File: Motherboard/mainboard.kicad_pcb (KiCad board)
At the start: 4 copper layers, 45 x 35 mm, 48 parts, among them IC1 BMX160, J1 Conn_01x01, J2 10118194-0001LF, J28 Conn_01x01, J29 Conn_01x01, J3 Micro_SD_Card, J30 Conn_01x01, J4 xf2m-2415-1a, J5 XF2M-1015-1A, SW1 KMR231NG LFS, U1 RFM95W-915S2, U2 ATSAMD51G_TQFN48, U3 DRV8848, U4 TPS82740BSIPR, U5 DRV8848, U6 MAX708RESA-T, U8 RFM95W-915S2, X1 ANTENNA_U.FL, X2 ANTENNA_U.FL

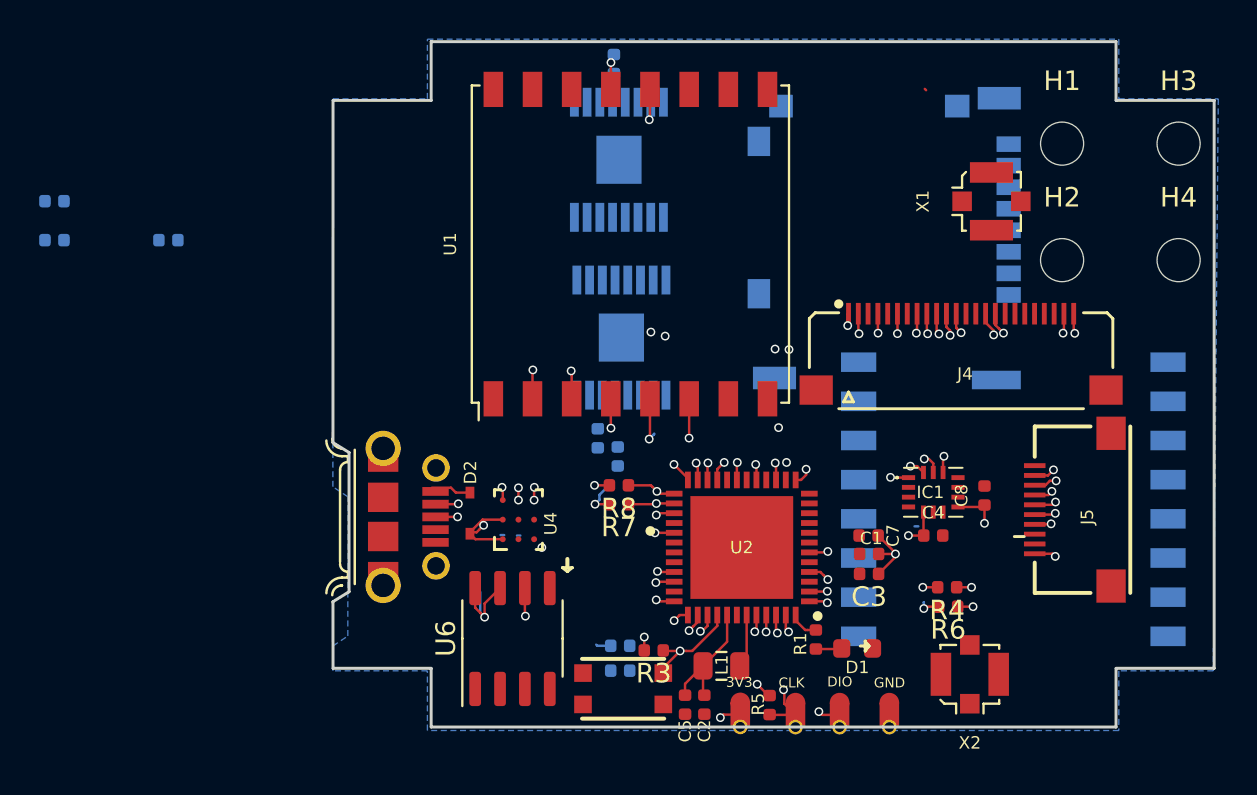
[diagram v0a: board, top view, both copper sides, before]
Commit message: updated H-bridge positions on bottom layer
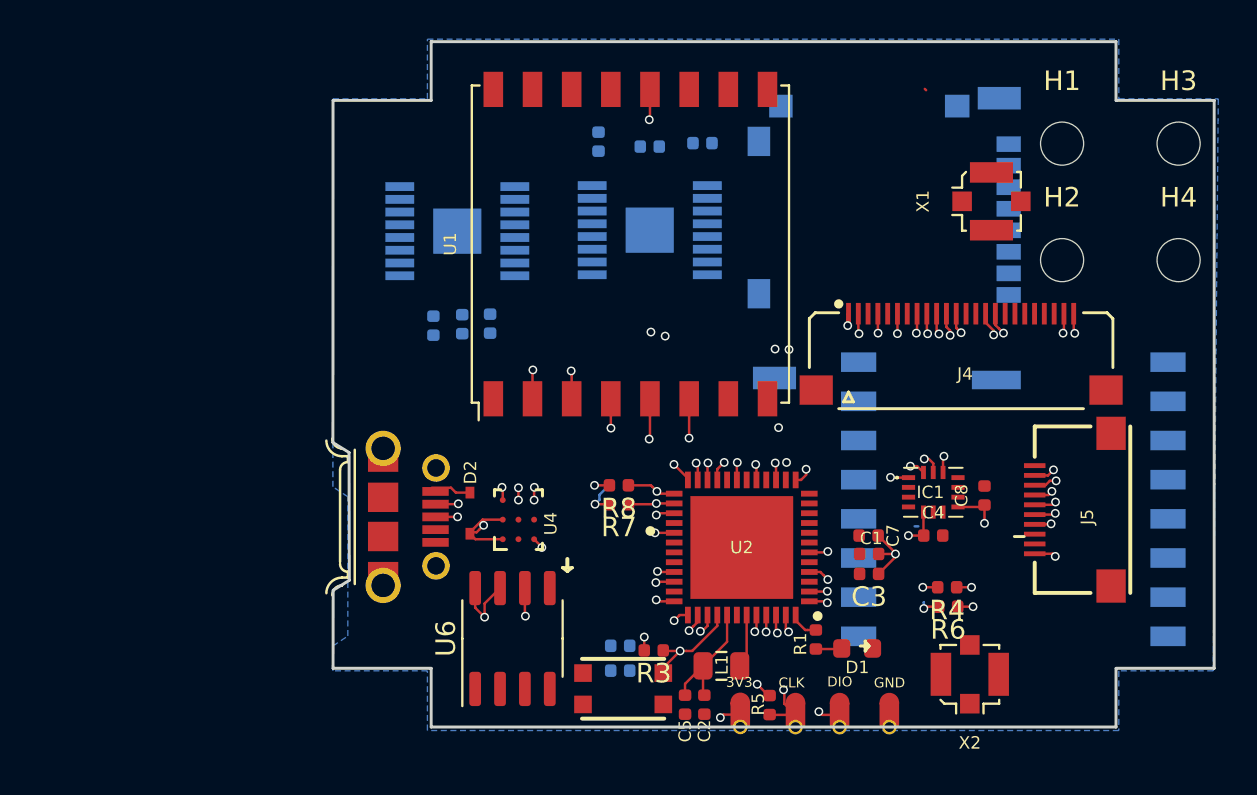
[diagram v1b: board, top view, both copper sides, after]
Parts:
- moved C9 33.5 mm to (95.6, 79.2)
- moved C11 30.5 mm to (92.9, 79.4)
- moved C14 17.0 mm to (84.7, 88.4), turned to 90 degrees
- moved C12 10.4 mm to (83.3, 88.5)
- moved C13 10.2 mm to (81.8, 88.5)
- moved U5 9.99 mm to (83.1, 83.7), turned to 0 degrees
- moved C10 4.04 mm to (90.3, 79.1)
- moved U3 3.92 mm to (92.9, 83.7), turned to 180 degrees
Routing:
- net Net-(C10-Pad1): track 1.50 -> 0.00 mm
- net Net-(R3-Pad2): track 14.3 -> 12.9 mm
- net +3V3: track 21.0 -> 20.2 mm, vias 16 -> 15
- net GND: track 0.79 -> 0.00 mm
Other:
- outline, holes or cut-outs redrawn

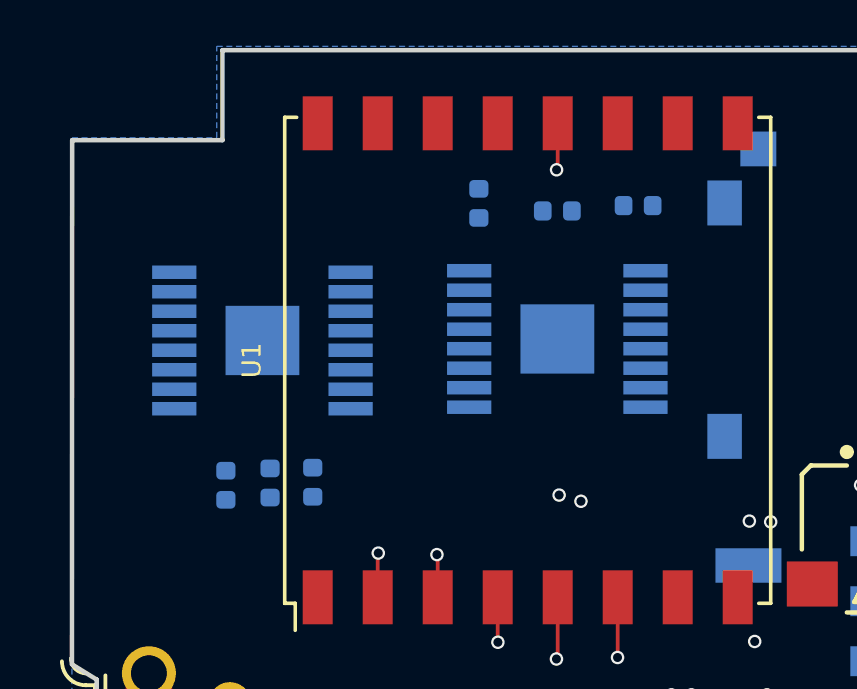
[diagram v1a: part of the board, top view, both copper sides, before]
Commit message: updated H-bridge positions traces with capacitors on bottom layer
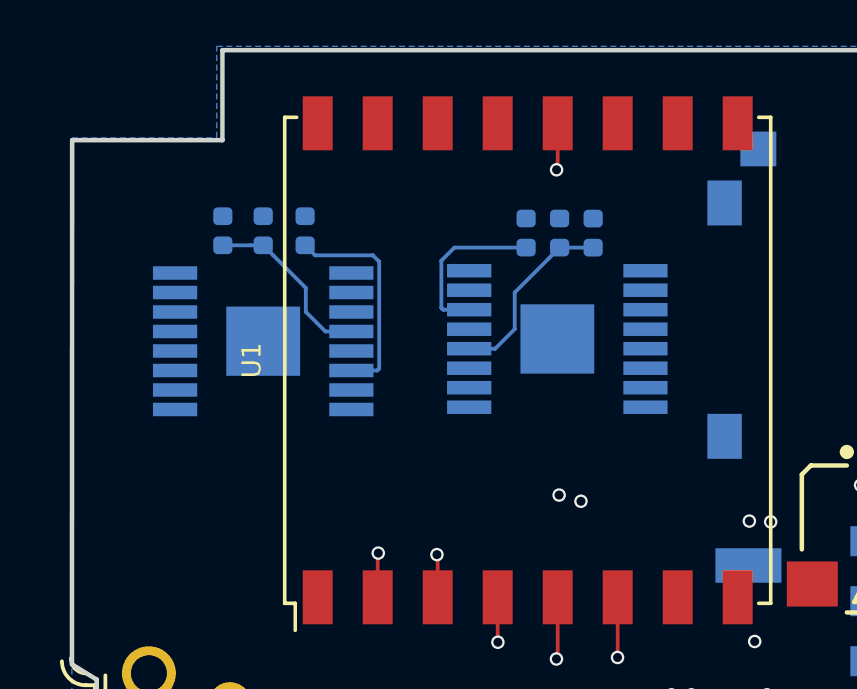
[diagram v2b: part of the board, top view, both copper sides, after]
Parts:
- moved C14 8.90 mm to (81.7, 80.1)
- moved C13 8.89 mm to (84.5, 80.1), turned to 270 degrees
- moved C12 8.41 mm to (83.1, 80.1), turned to 90 degrees
- moved C10 3.94 mm to (94.1, 80.1)
- moved C9 2.77 mm to (93.0, 80.1), turned to 90 degrees
- moved C11 1.28 mm to (91.8, 80.1), turned to 270 degrees
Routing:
- net Net-(C13-Pad2): track 0.00 -> 7.21 mm
- net Net-(C10-Pad1): track 0.00 -> 6.24 mm
- net Net-(C12-Pad1): track 0.00 -> 5.94 mm
- net Net-(C11-Pad2): track 0.00 -> 5.53 mm

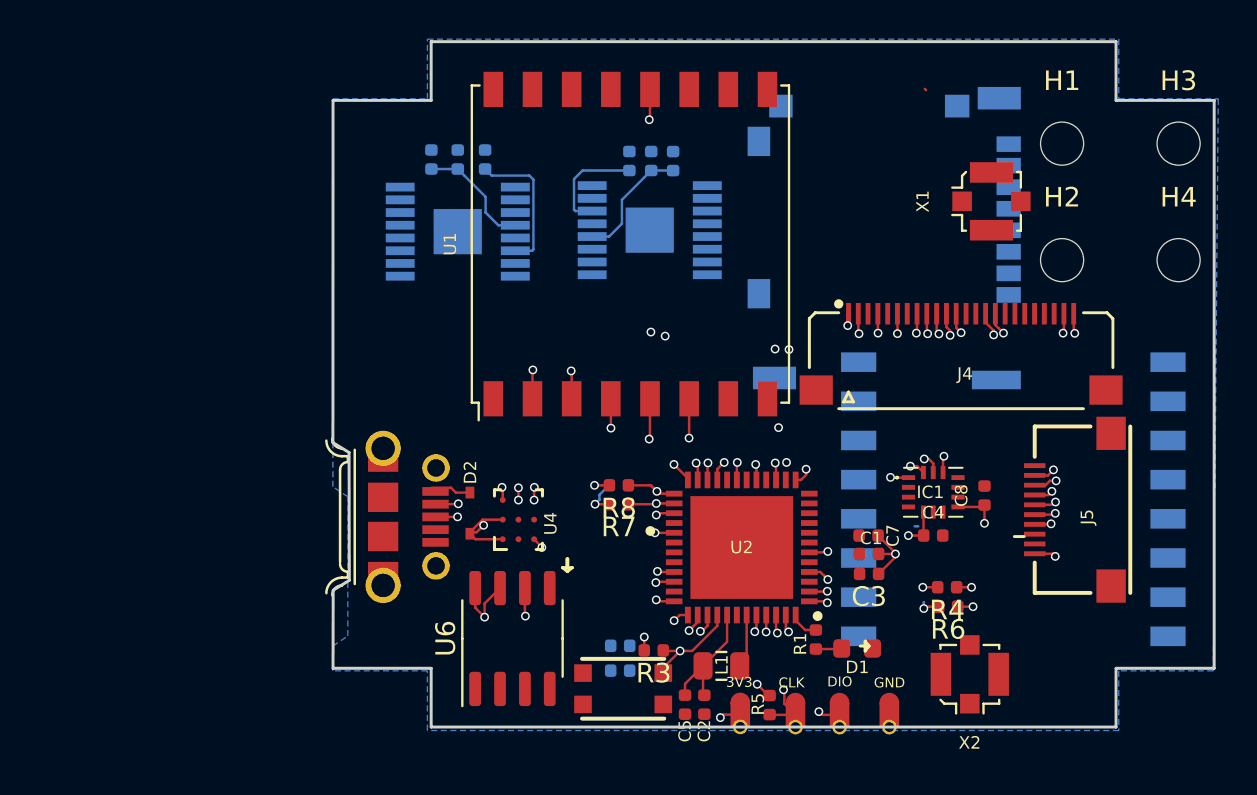
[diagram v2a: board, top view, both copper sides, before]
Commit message: updated traces for UHF and SD card on bottom layer
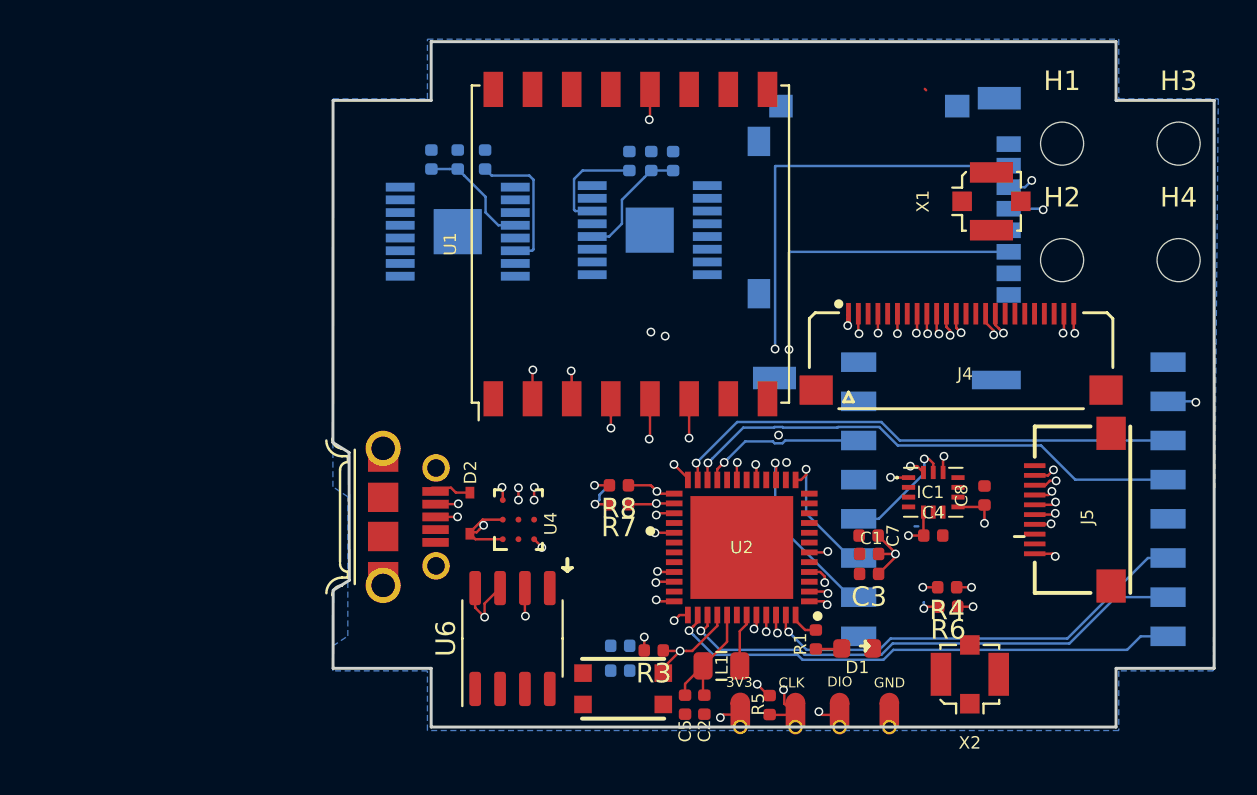
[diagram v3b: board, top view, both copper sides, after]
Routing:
- net MISO: track 38.0 -> 68.2 mm
- net RF_DIO2: track 0.98 -> 26.5 mm
- net RF_DIO1: track 1.03 -> 26.6 mm
- net RF_BUSY: track 0.88 -> 26.3 mm
- net RF_DIO3: track 0.90 -> 26.3 mm
- net MOSI: track 35.6 -> 57.7 mm
- net RF_DIO0: track 0.92 -> 22.6 mm
- net SCK: track 28.3 -> 48.7 mm, vias 5 -> 6
- net RF_RST: track 1.05 -> 8.45 mm
- net GND: track 0.00 -> 2.76 mm, vias 0 -> 2
